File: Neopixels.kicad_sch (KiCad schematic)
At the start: 12 parts

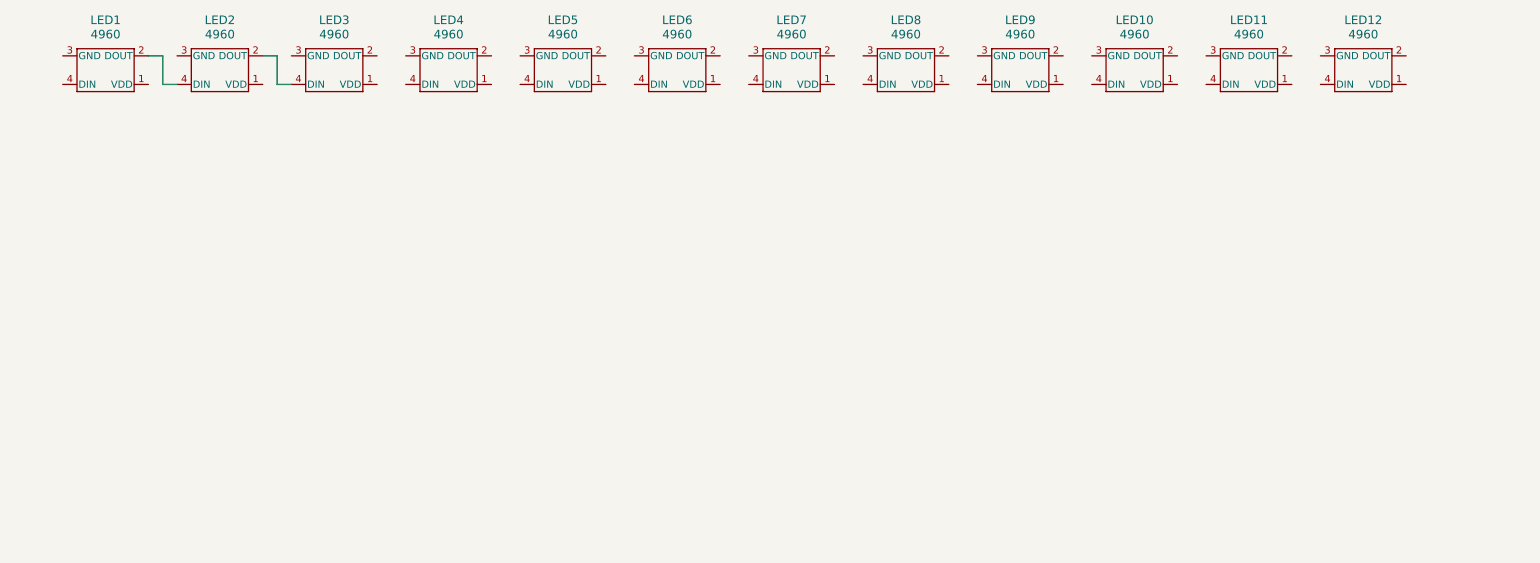
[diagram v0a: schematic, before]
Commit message: Place keyswitches in grid
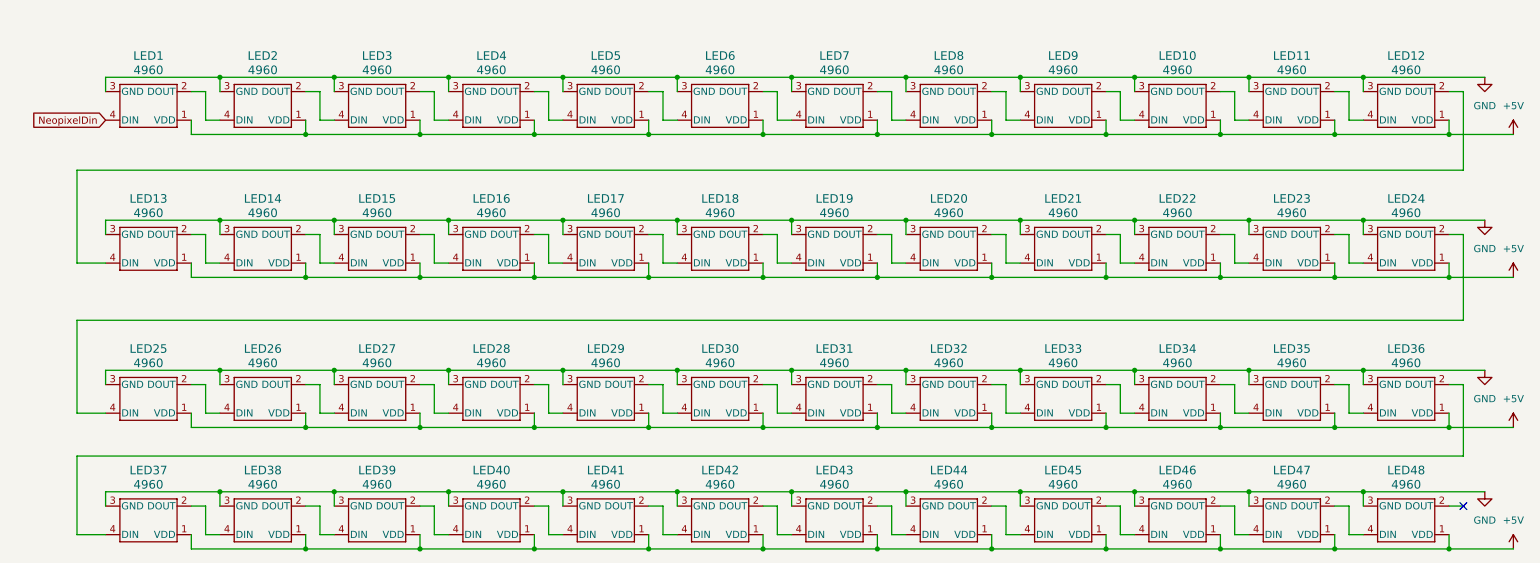
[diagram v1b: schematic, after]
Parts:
- added LED13, LED14, LED15, LED16, LED17, LED18, LED19, LED20, LED21, LED22, LED23, LED24, LED25, LED26, LED27, LED28, LED29, LED30, LED31, LED32, LED33, LED34, LED35, LED36, LED37, LED38, LED39, LED40, LED41, LED42, LED43, LED44, LED45, LED46, LED47, LED48: 4960, kbd:YS-SK6812MINI-E, symbol SK6812 Reverse mount:4960
- LED1, LED10, LED11, LED12, LED2, LED3, LED4, LED5, LED6, LED7, LED8, LED9: footprint 4960_ADA -> kbd:YS-SK6812MINI-E
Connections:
- net +5V: now reaches LED8.1 (VDD)
- net +5V: now also LED1.1 (VDD), LED10.1 (VDD), LED11.1 (VDD), LED12.1 (VDD), LED2.1 (VDD), LED3.1 (VDD), LED4.1 (VDD), LED5.1 (VDD), LED6.1 (VDD), LED7.1 (VDD), LED9.1 (VDD), LED13.1 (VDD), LED14.1 (VDD), LED15.1 (VDD), LED16.1 (VDD), LED17.1 (VDD), LED18.1 (VDD), LED19.1 (VDD), LED20.1 (VDD), LED21.1 (VDD), LED22.1 (VDD), LED23.1 (VDD), LED24.1 (VDD), LED25.1 (VDD), LED26.1 (VDD), LED27.1 (VDD), LED28.1 (VDD), LED29.1 (VDD), LED30.1 (VDD), LED31.1 (VDD), LED32.1 (VDD), LED33.1 (VDD), LED34.1 (VDD), LED35.1 (VDD), LED36.1 (VDD), LED37.1 (VDD), LED38.1 (VDD), LED39.1 (VDD), LED40.1 (VDD), LED41.1 (VDD), LED42.1 (VDD), LED43.1 (VDD), LED44.1 (VDD), LED45.1 (VDD), LED46.1 (VDD), LED47.1 (VDD), LED48.1 (VDD)
- net at LED8.2 (DOUT): now also LED9.4 (DIN)
- net GND: now reaches LED8.3 (GND)
- net GND: now also LED1.3 (GND), LED10.3 (GND), LED11.3 (GND), LED12.3 (GND), LED2.3 (GND), LED3.3 (GND), LED4.3 (GND), LED5.3 (GND), LED6.3 (GND), LED7.3 (GND), LED9.3 (GND), LED13.3 (GND), LED14.3 (GND), LED15.3 (GND), LED16.3 (GND), LED17.3 (GND), LED18.3 (GND), LED19.3 (GND), LED20.3 (GND), LED21.3 (GND), LED22.3 (GND), LED23.3 (GND), LED24.3 (GND), LED25.3 (GND), LED26.3 (GND), LED27.3 (GND), LED28.3 (GND), LED29.3 (GND), LED30.3 (GND), LED31.3 (GND), LED32.3 (GND), LED33.3 (GND), LED34.3 (GND), LED35.3 (GND), LED36.3 (GND), LED37.3 (GND), LED38.3 (GND), LED39.3 (GND), LED40.3 (GND), LED41.3 (GND), LED42.3 (GND), LED43.3 (GND), LED44.3 (GND), LED45.3 (GND), LED46.3 (GND), LED47.3 (GND), LED48.3 (GND)
- net at LED8.4 (DIN): now also LED7.2 (DOUT)
- net at LED7.4 (DIN): now also LED6.2 (DOUT)
- net at LED6.4 (DIN): now also LED5.2 (DOUT)
- net at LED12.2 (DOUT): now also LED13.4 (DIN)
- net at LED12.4 (DIN): now also LED11.2 (DOUT)
- net at LED10.2 (DOUT): now also LED11.4 (DIN)
- net at LED10.4 (DIN): now also LED9.2 (DOUT)
- net at LED5.4 (DIN): now also LED4.2 (DOUT)
- net at LED3.2 (DOUT): now also LED4.4 (DIN)
- net NeopixelDin: now reaches LED1.4 (DIN)
- new net: LED27.2 (DOUT), LED28.4 (DIN)
- new net: LED26.2 (DOUT), LED27.4 (DIN)
- new net: LED47.2 (DOUT), LED48.4 (DIN)
- new net: LED14.2 (DOUT), LED15.4 (DIN)
- new net: LED13.2 (DOUT), LED14.4 (DIN)
- new net: LED20.2 (DOUT), LED21.4 (DIN)
- new net: LED19.2 (DOUT), LED20.4 (DIN)
- new net: LED41.2 (DOUT), LED42.4 (DIN)
- new net: LED40.2 (DOUT), LED41.4 (DIN)
- new net: LED44.2 (DOUT), LED45.4 (DIN)
- new net: LED43.2 (DOUT), LED44.4 (DIN)
- new net: LED30.2 (DOUT), LED31.4 (DIN)
- new net: LED29.2 (DOUT), LED30.4 (DIN)
- new net: LED28.2 (DOUT), LED29.4 (DIN)
- new net: LED25.2 (DOUT), LED26.4 (DIN)
- new net: LED24.2 (DOUT), LED25.4 (DIN)
- new net: LED42.2 (DOUT), LED43.4 (DIN)
- new net: LED21.2 (DOUT), LED22.4 (DIN)
- new net: LED18.2 (DOUT), LED19.4 (DIN)
- new net: LED32.2 (DOUT), LED33.4 (DIN)
- new net: LED31.2 (DOUT), LED32.4 (DIN)
- new net: LED37.2 (DOUT), LED38.4 (DIN)
- new net: LED36.2 (DOUT), LED37.4 (DIN)
- new net: LED38.2 (DOUT), LED39.4 (DIN)
- new net: LED45.2 (DOUT), LED46.4 (DIN)
- new net: LED16.2 (DOUT), LED17.4 (DIN)
- new net: LED15.2 (DOUT), LED16.4 (DIN)
- new net: LED46.2 (DOUT), LED47.4 (DIN)
- new net: LED35.2 (DOUT), LED36.4 (DIN)
- new net: LED17.2 (DOUT), LED18.4 (DIN)
- new net: LED34.2 (DOUT), LED35.4 (DIN)
- new net: LED33.2 (DOUT), LED34.4 (DIN)
- new net: LED22.2 (DOUT), LED23.4 (DIN)
- new net: LED39.2 (DOUT), LED40.4 (DIN)
- new net: LED23.2 (DOUT), LED24.4 (DIN)
- no-connect marks 0 -> 1
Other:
- moved on the sheet: LED1, LED10, LED11, LED12, LED2, LED3, LED4, LED5, LED6, LED7, LED8, LED9

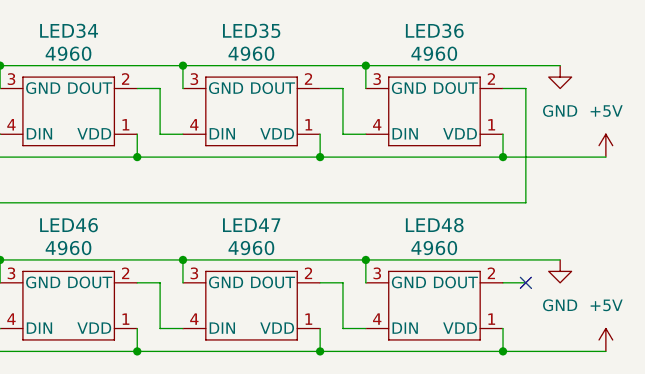
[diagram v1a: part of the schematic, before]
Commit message: Place LEDs
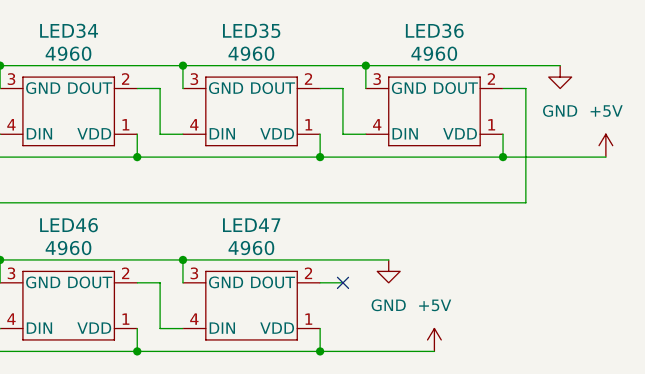
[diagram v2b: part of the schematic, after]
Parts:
- removed LED48: 4960, kbd:YS-SK6812MINI-E, symbol SK6812 Reverse mount:4960
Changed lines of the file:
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@@
 	)
 	(junction
-		(at 231.14 99.06)
-		(diameter 0)
-		(color 0 0 0 0)
-	)
-	(junction
 		(at 170.18 77.47)
 		(diameter 0)
@@
 	)
 	(junction
-		(at 266.7 109.22)
-		(diameter 0)
-		(color 0 0 0 0)
-	)
-	(junction
 		(at 149.86 77.47)
 		(diameter 0)
@@
 	)
 	(junction
+		(at 246.38 109.22)
+		(diameter 0)
+		(color 0 0 0 0)
+	)
+	(junction
 		(at 149.86 99.06)
 		(diameter 0)
@@
 	)
 	(junction
-		(at 185.42 109.22)
+		(at 231.14 99.06)
 		(diameter 0)
 		(color 0 0 0 0)
 	)
 	(junction
-		(at 104.14 35.56)
+		(at 185.42 109.22)
 		(diameter 0)
 		(color 0 0 0 0)
 	)
 	(junction
-		(at 246.38 109.22)
+		(at 104.14 35.56)
 		(diameter 0)
 		(color 0 0 0 0)
@@
 	)
 	(junction
-		(at 251.46 99.06)
-		(diameter 0)
-		(color 0 0 0 0)
-	)
-	(junction
 		(at 129.54 25.4)
 		(diameter 0)
@@
 	)
 	(no_connect
-		(at 269.24 101.6)
+		(at 248.92 101.6)
 	)
 	(wire
@@
 	(wire
 		(pts
-			(xy 248.92 106.68) (xy 251.46 106.68)
-		)
-		(stroke
-			(width 0)
-			(type default)
-		)
-	)
-	(wire
-		(pts
 			(xy 266.7 33.02) (xy 266.7 35.56)
 		)
@@
 	(wire
 		(pts
-			(xy 231.14 99.06) (xy 251.46 99.06)
+			(xy 231.14 99.06) (xy 254 99.06)
 		)
 		(stroke
@@
 	(wire
 		(pts
-			(xy 266.7 109.22) (xy 278.13 109.22)
+			(xy 246.38 109.22) (xy 259.08 109.22)
 		)
 		(stroke
@@
 	(wire
 		(pts
-			(xy 266.7 106.68) (xy 266.7 109.22)
-		)
-		(stroke
-			(width 0)
-			(type default)
-		)
-	)
-	(wire
-		(pts
 			(xy 144.78 58.42) (xy 144.78 60.96)
 		)
@@
 	(wire
 		(pts
-			(xy 266.7 101.6) (xy 269.24 101.6)
-		)
-		(stroke
-			(width 0)
-			(type default)
-		)
-	)
-	(wire
-		(pts
 			(xy 27.94 77.47) (xy 48.26 77.47)
 		)
@@
 	(wire
 		(pts
-			(xy 248.92 101.6) (xy 248.92 106.68)
-		)
-		(stroke
-			(width 0)
-			(type default)
-		)
-	)
-	(wire
-		(pts
 			(xy 170.18 50.8) (xy 190.5 50.8)
 		)
@@
 	(wire
 		(pts
-			(xy 246.38 109.22) (xy 266.7 109.22)
-		)
-		(stroke
-			(width 0)
-			(type default)
-		)
-	)
-	(wire
-		(pts
 			(xy 231.14 77.47) (xy 251.46 77.47)
 		)
@@
 	(wire
 		(pts
-			(xy 251.46 101.6) (xy 251.46 99.06)
-		)
-		(stroke
-			(width 0)
-			(type default)
-		)
-	)
-	(wire
-		(pts
 			(xy 231.14 50.8) (xy 251.46 50.8)
 		)
@@
 	(wire
 		(pts
-			(xy 251.46 99.06) (xy 273.05 99.06)
-		)
-		(stroke
-			(width 0)
-			(type default)
-		)
-	)
-	(wire
-		(pts
 			(xy 266.7 58.42) (xy 266.7 60.96)
 		)
@@
 	)
 	(symbol
-		(lib_id "SK6812 Reverse mount:4960")
-		(at 259.08 104.14 180)
-		(unit 1)
-		(body_style 1)
-		(exclude_from_sim no)
-		(in_bom yes)
-		(on_board yes)
-		(in_pos_files yes)
-		(dnp no)
-		(fields_autoplaced yes)
-		(property "Reference" "LED48"
-			(at 259.08 95.25 0)
-			(show_name no)
-			(do_not_autoplace no)
-			(effects
-				(font
-					(size 1.524 1.524)
-				)
-			)
-		)
-		(property "Value" "4960"
-			(at 259.08 97.79 0)
-			(show_name no)
-			(do_not_autoplace no)
-			(effects
-				(font
-					(size 1.524 1.524)
-				)
-			)
-		)
-		(property "Footprint" "kbd:YS-SK6812MINI-E"
-			(at 259.08 104.14 0)
-			(hide yes)
-			(show_name no)
-			(do_not_autoplace no)
-			(effects
-				(font
-					(size 1.27 1.27)
-					(italic yes)
-				)
-			)
-		)
-		(property "Datasheet" "4960"
-			(at 261.366 104.14 0)
-			(hide yes)
-			(show_name no)
-			(do_not_autoplace no)
-			(effects
-				(font
-					(size 1.27 1.27)
-					(italic yes)
-				)
-			)
-		)
-		(property "Description" ""
-			(at 259.08 104.14 0)
-			(hide yes)
-			(show_name no)
-			(do_not_autoplace no)
-			(effects
-				(font
-					(size 1.27 1.27)
-				)
-			)
-		)
-		(property "JLCPCB Part #" ""
-			(at 259.08 104.14 0)
-			(hide yes)
-			(show_name no)
-			(do_not_autoplace no)
-			(effects
-				(font
-					(size 1.27 1.27)
-				)
-			)
-		)
-		(property "MFR.Part #" ""
-			(at 259.08 104.14 0)
-			(hide yes)
-			(show_name no)
-			(do_not_autoplace no)
-			(effects
-				(font
-					(size 1.27 1.27)
-				)
-			)
-		)
-		(pin "1"
-		)
-		(pin "4"
-		)
-		(pin "3"
-		)
-		(pin "2"
-		)
-		(instances
-			(project "Contra"
-				(path "/490ed6d6-ce6d-4821-aa52-98b9130151cb/a1594013-5f39-4e11-a3d4-58e2ccc1ee5f"
-					(reference "LED48")
-					(unit 1)
-				)
-			)
-		)
-	)
-	(symbol
 		(lib_id "power:+5V")
 		(at 278.13 87.63 0)
@@
 	(symbol
 		(lib_id "power:GND")
-		(at 273.05 99.06 0)
+		(at 254 99.06 0)
 		(unit 1)
 		(body_style 1)
@@
 		(fields_autoplaced yes)
 		(property "Reference" "#PWR014"
-			(at 273.05 105.41 0)
+			(at 254 105.41 0)
 			(hide yes)
 			(show_name no)
@@
 		)
 		(property "Value" "GND"
-			(at 273.05 104.14 0)
+			(at 254 104.14 0)
 			(show_name no)
 			(do_not_autoplace no)
@@
 		)
 		(property "Footprint" ""
-			(at 273.05 99.06 0)
+			(at 254 99.06 0)
 			(hide yes)
 			(show_name no)
@@
 		)
 		(property "Datasheet" ""
-			(at 273.05 99.06 0)
+			(at 254 99.06 0)
 			(hide yes)
 			(show_name no)
@@
 		)
 		(property "Description" "Power symbol creates a global label with name \"GND\" , ground"
-			(at 273.05 99.06 0)
+			(at 254 99.06 0)
 			(hide yes)
 			(show_name no)
@@
 	(symbol
 		(lib_id "power:+5V")
-		(at 278.13 109.22 0)
+		(at 259.08 109.22 0)
 		(unit 1)
 		(body_style 1)
@@
 		(fields_autoplaced yes)
 		(property "Reference" "#PWR015"
-			(at 278.13 113.03 0)
+			(at 259.08 113.03 0)
 			(hide yes)
 			(show_name no)
@@
 		)
 		(property "Value" "+5V"
-			(at 278.13 104.14 0)
+			(at 259.08 104.14 0)
 			(show_name no)
 			(do_not_autoplace no)
@@
 		)
 		(property "Footprint" ""
-			(at 278.13 109.22 0)
+			(at 259.08 109.22 0)
 			(hide yes)
 			(show_name no)
@@
 		)
 		(property "Datasheet" ""
-			(at 278.13 109.22 0)
+			(at 259.08 109.22 0)
 			(hide yes)
 			(show_name no)
@@
 		)
 		(property "Description" "Power symbol creates a global label with name \"+5V\""
-			(at 278.13 109.22 0)
+			(at 259.08 109.22 0)
 			(hide yes)
 			(show_name no)

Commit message: change +5V to VBAT
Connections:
- net +5V renamed VBAT
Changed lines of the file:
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@@
 			)
 		)
-		(property "Value" "+5V"
+		(property "Value" "VBAT"
 			(at 278.13 82.55 0)
 			(show_name no)
@@
 			)
 		)
-		(property "Value" "+5V"
+		(property "Value" "VBAT"
 			(at 259.08 104.14 0)
 			(show_name no)
@@
 			)
 		)
-		(property "Value" "+5V"
+		(property "Value" "VBAT"
 			(at 278.13 55.88 0)
 			(show_name no)
@@
 			)
 		)
-		(property "Value" "+5V"
+		(property "Value" "VBAT"
 			(at 278.13 30.48 0)
 			(show_name no)
